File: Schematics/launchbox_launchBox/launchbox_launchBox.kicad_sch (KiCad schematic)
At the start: 15 parts, among them J1 Screw_Terminal_01x02, J2 Screw_Terminal_01x02, J3 Msg_Recv_LED, J4 Rail_isArmed_LED, J5 Radio_power, J6 Radio_rx_tx, SW1 Arm_switch, SW2 fire_btn, SW3 Batt_on_off

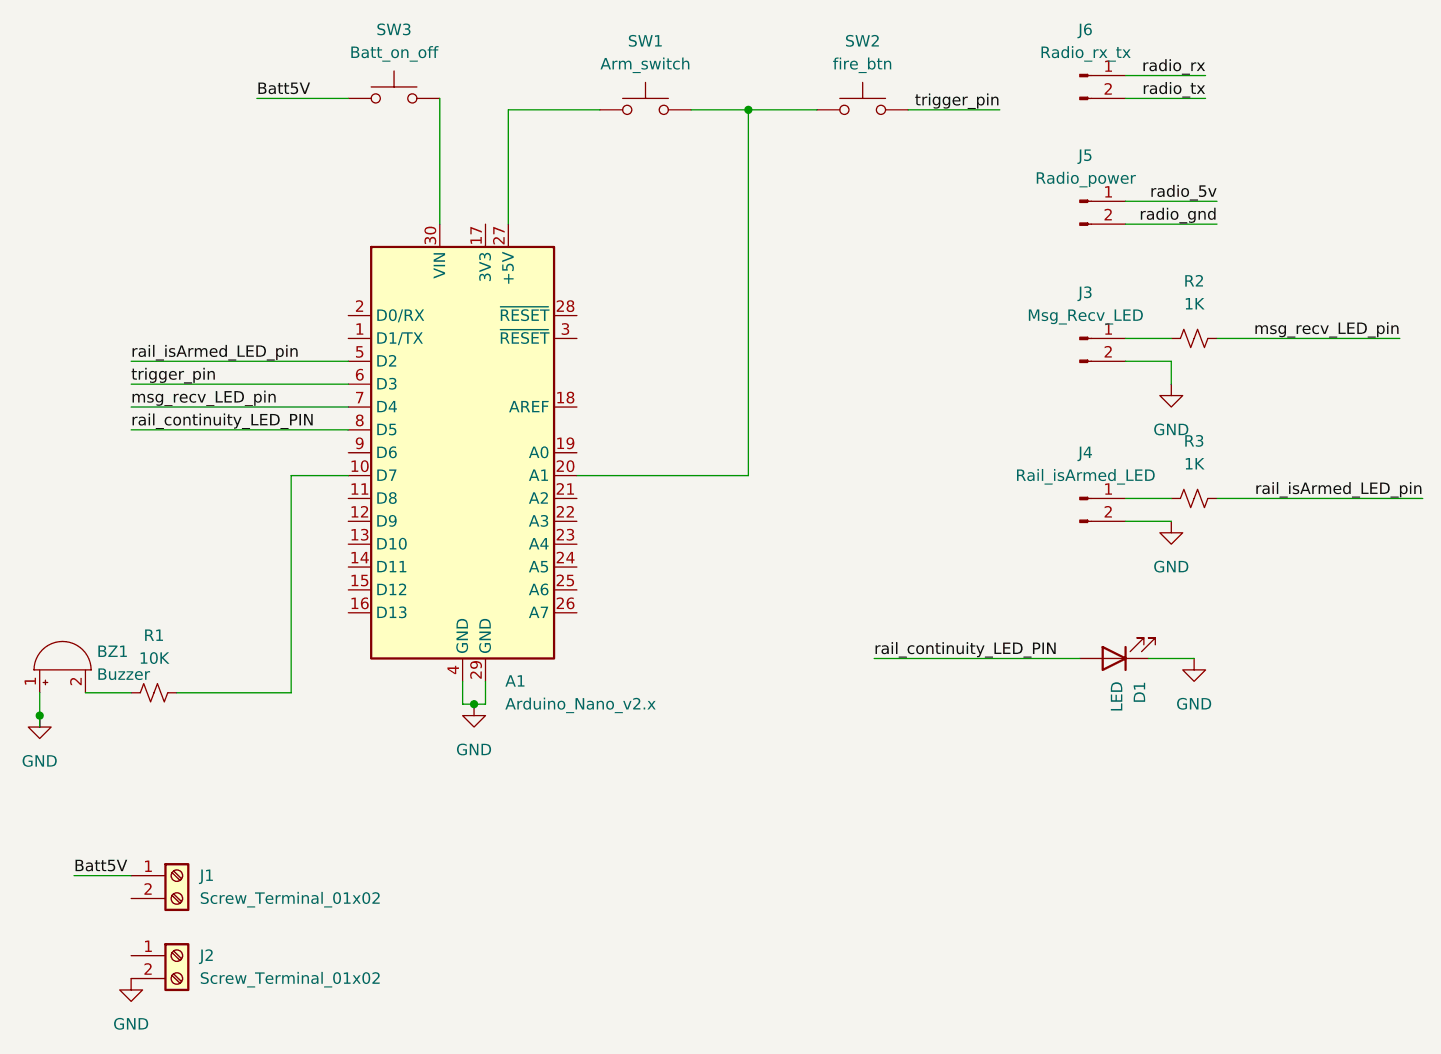
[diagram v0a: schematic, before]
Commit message: Updating Handheld PCB
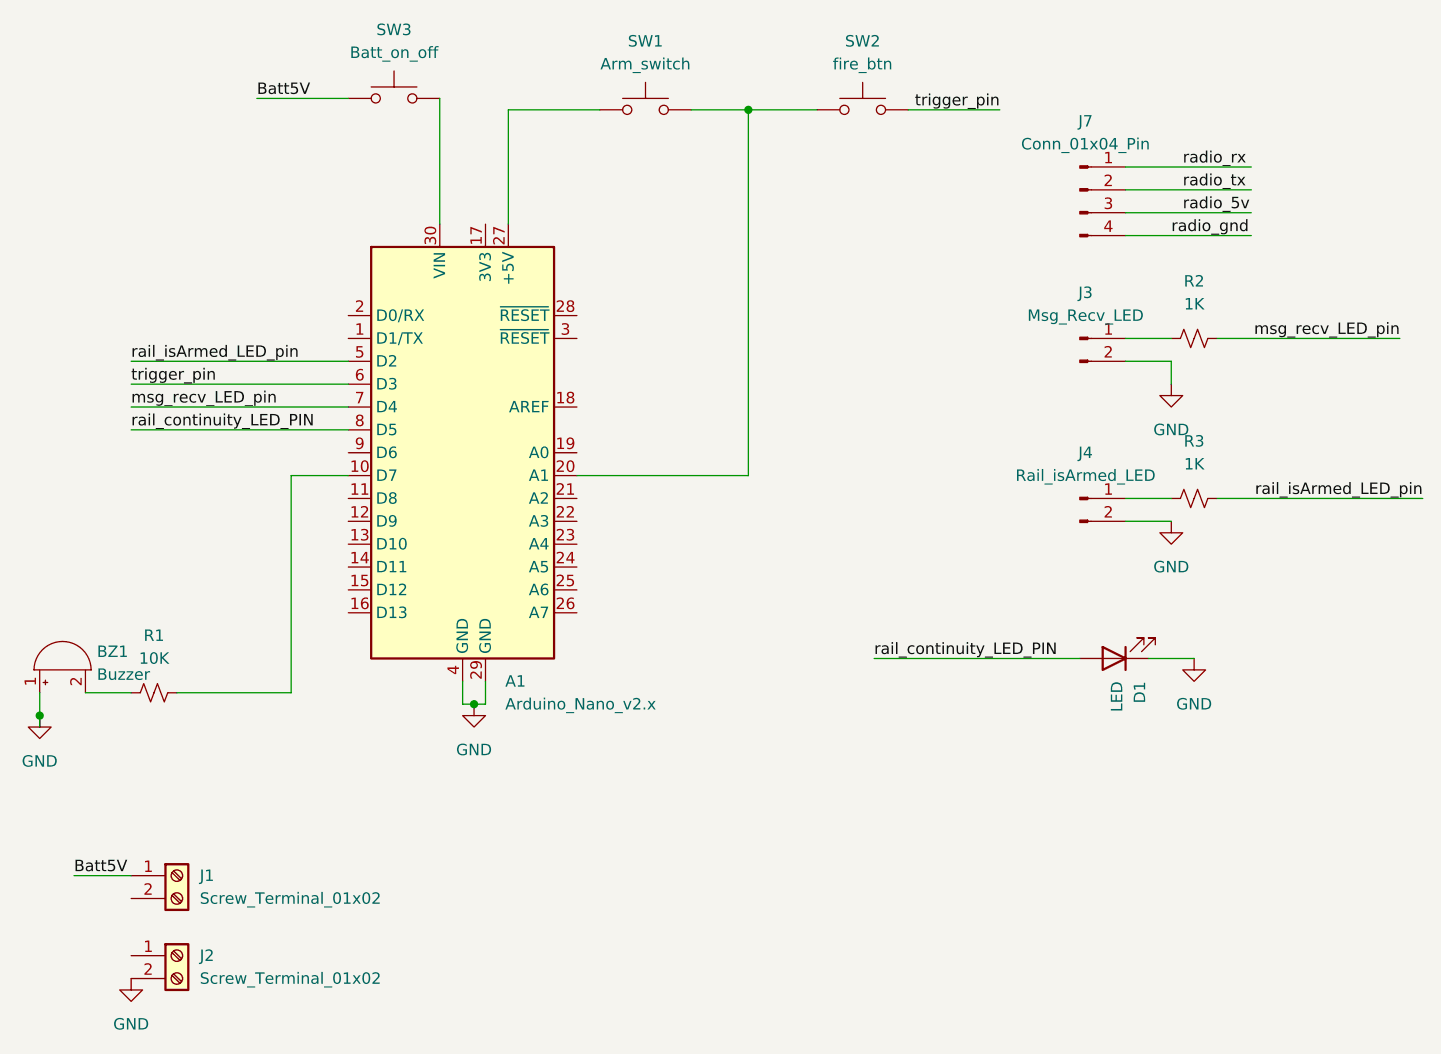
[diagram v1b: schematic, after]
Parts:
- removed J5: Radio_power, Connector_PinHeader_2.54mm:PinHeader_1x02_P2.54mm_Vertical, symbol Connector:Conn_01x02_Pin
- removed J6: Radio_rx_tx, Connector_PinHeader_2.54mm:PinHeader_1x02_P2.54mm_Vertical, symbol Connector:Conn_01x02_Pin
- added J7: Conn_01x04_Pin, Connector_PinHeader_2.54mm:PinHeader_1x04_P2.54mm_Vertical, symbol Connector:Conn_01x04_Pin
- R1, R2, R3: footprint (none) -> Resistor_SMD:R_0603_1608Metric_Pad0.98x0.95mm_HandSolder
- SW1, SW2, SW3: footprint (none) -> Connector_PinHeader_2.54mm:PinHeader_1x02_P2.54mm_Vertical
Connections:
- net radio_5v: now also J7.3 (Pin_3)
- net radio_gnd: now also J7.4 (Pin_4)
- net radio_rx: now also J7.1 (Pin_1)
- net radio_tx: now also J7.2 (Pin_2)

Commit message: completed launch box pcb
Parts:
- removed J1, J2: Screw_Terminal_01x02, symbol Connector:Screw_Terminal_01x02
- removed SW3: Batt_on_off, Connector_PinHeader_2.54mm:PinHeader_1x02_P2.54mm_Vertical, symbol Switch:SW_MEC_5G
- added H1, H2, H3, H4: MountingHole_Pad, MountingHole:MountingHole_3.2mm_M3_Pad_TopBottom, symbol Mechanical:MountingHole_Pad
- added J1: batt_switched_pwr, Connector_PinHeader_2.54mm:PinHeader_1x02_P2.54mm_Vertical, symbol Connector:Conn_01x02_Pin
- BZ1, D1: footprint (none) -> Connector_PinHeader_2.54mm:PinHeader_1x02_P2.54mm_Vertical
- renumbered J3 to J2, J4 to J3, J7 to J4
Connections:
- net radio_5v is gone; now on net nano_to_rad: J4.3 (Pin_2)
- net radio_gnd is gone; now on net rad_to_nano: J4.4 (Pin_1)
- net radio_rx is gone; now on net GND: J4.1 (Pin_4)
- net radio_tx is gone; now on net +5V: J4.2 (Pin_3)
- net GND: now also J2.1 (Pin_2), J3.1 (Pin_2), H1.1, H2.1, H3.1, H4.1, J1.1 (Pin_1); no longer J2.2 (Pin_2), J3.2 (Pin_2)
- net at R2.1: now also J2.2 (Pin_1); no longer J2.1 (Pin_1)
- net VIN: now reaches A1.30 (VIN)
- net VIN: now also J1.2 (Pin_2)
- net nano_to_rad: now reaches A1.1 (D1/TX)
- net rad_to_nano: now reaches A1.2 (D0/RX)
- net at A1.20 (A1), SW2.1: now also SW1.2 (B); no longer SW1.3 (B), SW1.4 (B)
- net +5V: now reaches A1.27 (+5V), SW1.1 (A)
- net +5V: no longer SW1.2 (A)
- net at R3.1: now also J3.2 (Pin_1); no longer J3.1 (Pin_1)
